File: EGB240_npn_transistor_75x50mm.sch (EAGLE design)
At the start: 12 parts, among them Q1 2N4126, U1 74HC14

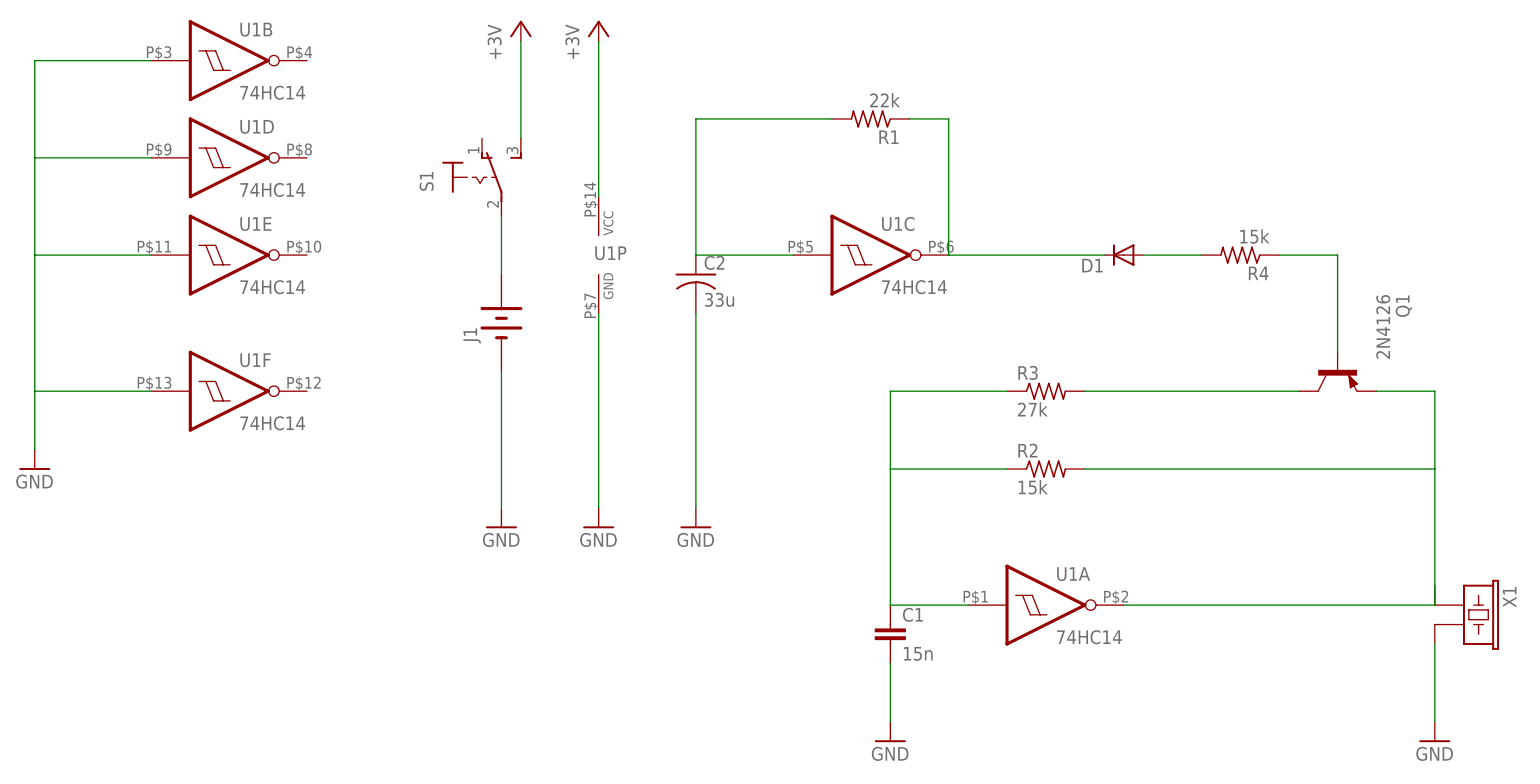
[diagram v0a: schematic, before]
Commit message: added npn board
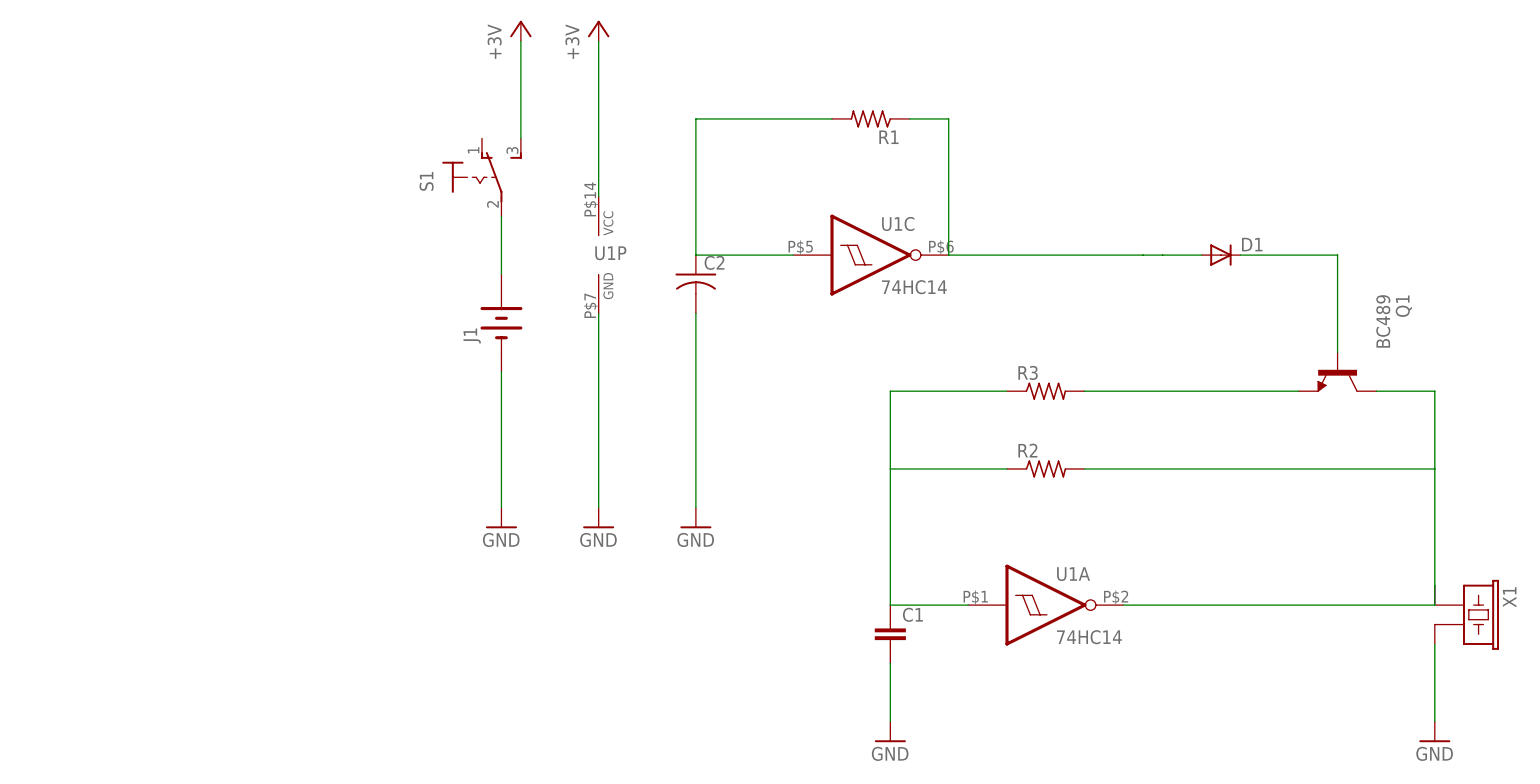
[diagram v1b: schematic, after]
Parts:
- removed R4: 15k, EGB240:RESISTOR-AXIALHORIZONTAL
- C1: value 15n -> (none)
- C2: value 33u -> (none)
- Q1: value 2N4126 -> BC489; device transistor-pnp:2N4126 -> transistor-npn:BC489
- R1: value 22k -> (none)
- R2: value 15k -> (none)
- R3: value 27k -> (none)
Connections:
- removed net N$3: D1.A, R4.2
- net GND: no longer U1B.I, U1D.I, U1E.I, U1F.I
- net N$2: now also D1.A; no longer D1.K
- net N$4: now also D1.K; no longer R4.1
- net N$5: now also Q1.E; no longer Q1.C
- net N$7: now also Q1.C; no longer Q1.E
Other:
- moved on the sheet: D1
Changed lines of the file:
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@@
 <parts>
 <part name="U1" library="EGB240" deviceset="74HC14" device=""/>
-<part name="R1" library="EGB240" deviceset="RESISTOR-AXIAL" device="VERTICAL" value="22k"/>
-<part name="R2" library="EGB240" deviceset="RESISTOR-AXIAL" device="VERTICAL" value="15k"/>
-<part name="C1" library="EGB240" deviceset="CAP" device="CERAMIC-DISC" value="15n"/>
+<part name="R1" library="EGB240" deviceset="RESISTOR-AXIAL" device="VERTICAL"/>
+<part name="R2" library="EGB240" deviceset="RESISTOR-AXIAL" device="VERTICAL"/>
+<part name="C1" library="EGB240" deviceset="CAP" device="CERAMIC-DISC"/>
 <part name="J1" library="EGB240" deviceset="BATTERY-3V" device="BATT"/>
 <part name="V+1" library="EGB240" deviceset="+3V" device=""/>
@@
 <part name="S1" library="EGB240" deviceset="SWITCH-SPDT" device=""/>
 <part name="X1" library="EGB240" deviceset="BUZZER-PIEZO" device="PS1720P02"/>
-<part name="C2" library="EGB240" deviceset="CAP-POL" device="RB-D5.0XP2.0" value="33u"/>
+<part name="C2" library="EGB240" deviceset="CAP-POL" device="RB-D5.0XP2.0"/>
 <part name="GND2" library="EGB240" deviceset="GND" device=""/>
 <part name="GND3" library="EGB240" deviceset="GND" device=""/>
 <part name="GND4" library="EGB240" deviceset="GND" device=""/>
-<part name="R3" library="EGB240" deviceset="RESISTOR-AXIAL" device="VERTICAL" value="27k"/>
-<part name="D1" library="EGB240" deviceset="DIODE-DO35" device="DO35-P2.54"/>
-<part name="R4" library="EGB240" deviceset="RESISTOR-AXIAL" device="HORIZONTAL" value="15k"/>
-<part name="Q1" library="transistor-pnp" deviceset="2N4126*" device=""/>
+<part name="R3" library="EGB240" deviceset="RESISTOR-AXIAL" device="VERTICAL"/>
 <part name="V+2" library="EGB240" deviceset="+3V" device=""/>
 <part name="GND5" library="EGB240" deviceset="GND" device=""/>
-<part name="GND6" library="EGB240" deviceset="GND" device=""/>
+<part name="D1" library="EGB240" deviceset="DIODE-DO35" device="DO35-P2.54"/>
+<part name="Q1" library="transistor-npn" deviceset="BC489*" device=""/>
 </parts>
 <sheets>
@@
 <instance part="GND4" gate="1" x="109.22" y="-10.16"/>
 <instance part="R3" gate="G$1" x="58.42" y="35.56"/>
-<instance part="D1" gate="G$1" x="68.58" y="53.34" rot="R180"/>
-<instance part="R4" gate="G$1" x="83.82" y="53.34" rot="R180"/>
-<instance part="Q1" gate="G$1" x="96.52" y="38.1" rot="R270"/>
 <instance part="U1" gate="P" x="0" y="53.34"/>
 <instance part="V+2" gate="1" x="0" y="83.82"/>
 <instance part="GND5" gate="1" x="0" y="17.78"/>
-<instance part="U1" gate="B" x="-48.26" y="78.74"/>
-<instance part="U1" gate="D" x="-48.26" y="66.04"/>
-<instance part="U1" gate="E" x="-48.26" y="53.34"/>
-<instance part="U1" gate="F" x="-48.26" y="35.56"/>
-<instance part="GND6" gate="1" x="-73.66" y="25.4"/>
+<instance part="D1" gate="G$1" x="81.28" y="53.34"/>
+<instance part="Q1" gate="G$1" x="96.52" y="38.1" rot="R270"/>
 </instances>
 <busses>
@@
 <wire x1="0" y1="45.72" x2="0" y2="20.32" width="0.1524" layer="91"/>
 </segment>
-<segment>
-<pinref part="GND6" gate="1" pin="GND"/>
-<wire x1="-73.66" y1="27.94" x2="-73.66" y2="35.56" width="0.1524" layer="91"/>
-<pinref part="U1" gate="B" pin="I"/>
-<wire x1="-73.66" y1="35.56" x2="-73.66" y2="53.34" width="0.1524" layer="91"/>
-<wire x1="-73.66" y1="53.34" x2="-73.66" y2="66.04" width="0.1524" layer="91"/>
-<wire x1="-73.66" y1="66.04" x2="-73.66" y2="78.74" width="0.1524" layer="91"/>
-<wire x1="-73.66" y1="78.74" x2="-58.42" y2="78.74" width="0.1524" layer="91"/>
-<pinref part="U1" gate="D" pin="I"/>
-<wire x1="-58.42" y1="66.04" x2="-73.66" y2="66.04" width="0.1524" layer="91"/>
-<pinref part="U1" gate="E" pin="I"/>
-<wire x1="-58.42" y1="53.34" x2="-73.66" y2="53.34" width="0.1524" layer="91"/>
-<pinref part="U1" gate="F" pin="I"/>
-<wire x1="-58.42" y1="35.56" x2="-73.66" y2="35.56" width="0.1524" layer="91"/>
-</segment>
 </net>
 <net name="N$2" class="0">
@@
 <wire x1="40.64" y1="71.12" x2="45.72" y2="71.12" width="0.1524" layer="91"/>
 <wire x1="45.72" y1="71.12" x2="45.72" y2="53.34" width="0.1524" layer="91"/>
-<pinref part="D1" gate="G$1" pin="K"/>
-<wire x1="45.72" y1="53.34" x2="66.04" y2="53.34" width="0.1524" layer="91"/>
-</segment>
-</net>
-<net name="N$3" class="0">
-<segment>
+<wire x1="45.72" y1="53.34" x2="71.12" y2="53.34" width="0.1524" layer="91"/>
+<wire x1="71.12" y1="53.34" x2="73.66" y2="53.34" width="0.1524" layer="91"/>
+<wire x1="73.66" y1="53.34" x2="78.74" y2="53.34" width="0.1524" layer="91"/>
 <pinref part="D1" gate="G$1" pin="A"/>
-<pinref part="R4" gate="G$1" pin="2"/>
-<wire x1="71.12" y1="53.34" x2="78.74" y2="53.34" width="0.1524" layer="91"/>
 </segment>
 </net>
 <net name="N$4" class="0">
 <segment>
-<pinref part="R4" gate="G$1" pin="1"/>
+<wire x1="96.52" y1="53.34" x2="96.52" y2="40.64" width="0.1524" layer="91"/>
+<pinref part="D1" gate="G$1" pin="K"/>
+<wire x1="83.82" y1="53.34" x2="96.52" y2="53.34" width="0.1524" layer="91"/>
 <pinref part="Q1" gate="G$1" pin="B"/>
-<wire x1="88.9" y1="53.34" x2="96.52" y2="53.34" width="0.1524" layer="91"/>
-<wire x1="96.52" y1="53.34" x2="96.52" y2="40.64" width="0.1524" layer="91"/>
 </segment>
 </net>
 <net name="N$5" class="0">
 <segment>
-<pinref part="Q1" gate="G$1" pin="C"/>
 <pinref part="R3" gate="G$1" pin="2"/>
 <wire x1="91.44" y1="35.56" x2="63.5" y2="35.56" width="0.1524" layer="91"/>
+<pinref part="Q1" gate="G$1" pin="E"/>
 </segment>
 </net>
@@
 <pinref part="X1" gate="G$1" pin="1"/>
 <wire x1="109.22" y1="25.4" x2="109.22" y2="10.16" width="0.1524" layer="91"/>
-<pinref part="Q1" gate="G$1" pin="E"/>
 <wire x1="101.6" y1="35.56" x2="109.22" y2="35.56" width="0.1524" layer="91"/>
 <wire x1="109.22" y1="35.56" x2="109.22" y2="25.4" width="0.1524" layer="91"/>
@@
 <wire x1="68.58" y1="7.62" x2="109.22" y2="7.62" width="0.1524" layer="91"/>
 <wire x1="109.22" y1="7.62" x2="109.22" y2="10.16" width="0.1524" layer="91"/>
+<pinref part="Q1" gate="G$1" pin="C"/>
 </segment>
 </net>
